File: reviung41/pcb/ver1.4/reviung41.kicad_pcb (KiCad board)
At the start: 2 copper layers, 253.3 x 107.1 mm, 111 parts, among them SW1 SW_PUSH, SW10 SW_PUSH, SW11 SW_PUSH, SW12 SW_PUSH, SW13 SW_PUSH, SW14 SW_PUSH, SW15 SW_PUSH, SW16 SW_PUSH, SW17 SW_PUSH, SW18 SW_PUSH, SW19 SW_PUSH, SW2 SW_PUSH, SW20 SW_PUSH, SW21 SW_PUSH, SW22 SW_PUSH, SW23 SW_PUSH, SW24 SW_PUSH, SW25 SW_PUSH, SW26 SW_PUSH, SW27 SW_PUSH, SW28 SW_PUSH, SW29 SW_PUSH, SW3 SW_PUSH, SW30 SW_PUSH, SW31 SW_PUSH, SW32 SW_PUSH, SW33 SW_PUSH, SW34 SW_PUSH, SW35 SW_PUSH, SW36 SW_PUSH, SW37 SW_PUSH, SW38 SW_PUSH, SW39 SW_2U_PUSH, SW4 SW_PUSH, SW40 SW_PUSH, SW41 SW_PUSH, SW5 SW_PUSH, SW6 SW_PUSH, SW7 SW_PUSH, SW8 SW_PUSH, SW9 SW_PUSH, U1 ProMicro

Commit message: Add KiCad 6 project for reviung41
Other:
- net class Default removed

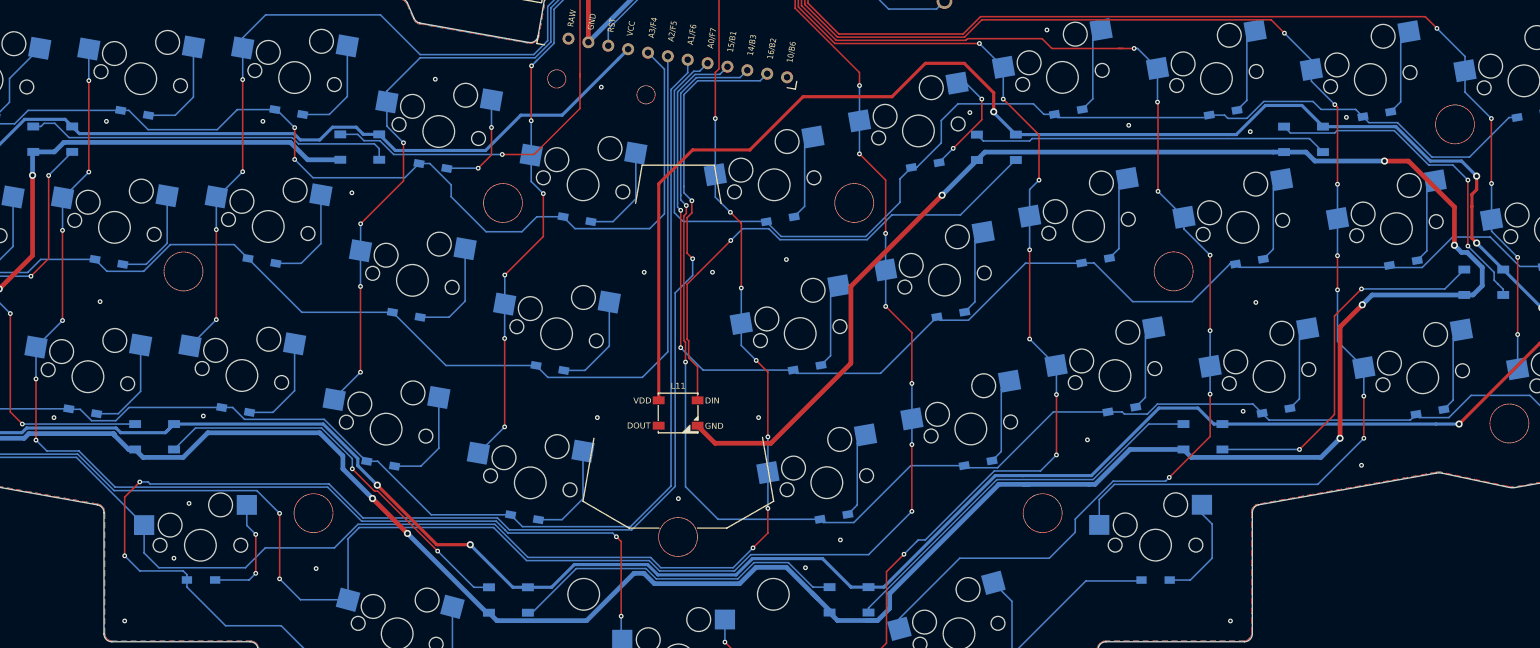
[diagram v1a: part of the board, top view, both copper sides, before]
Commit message: Cleanup zero length and redundant tracks
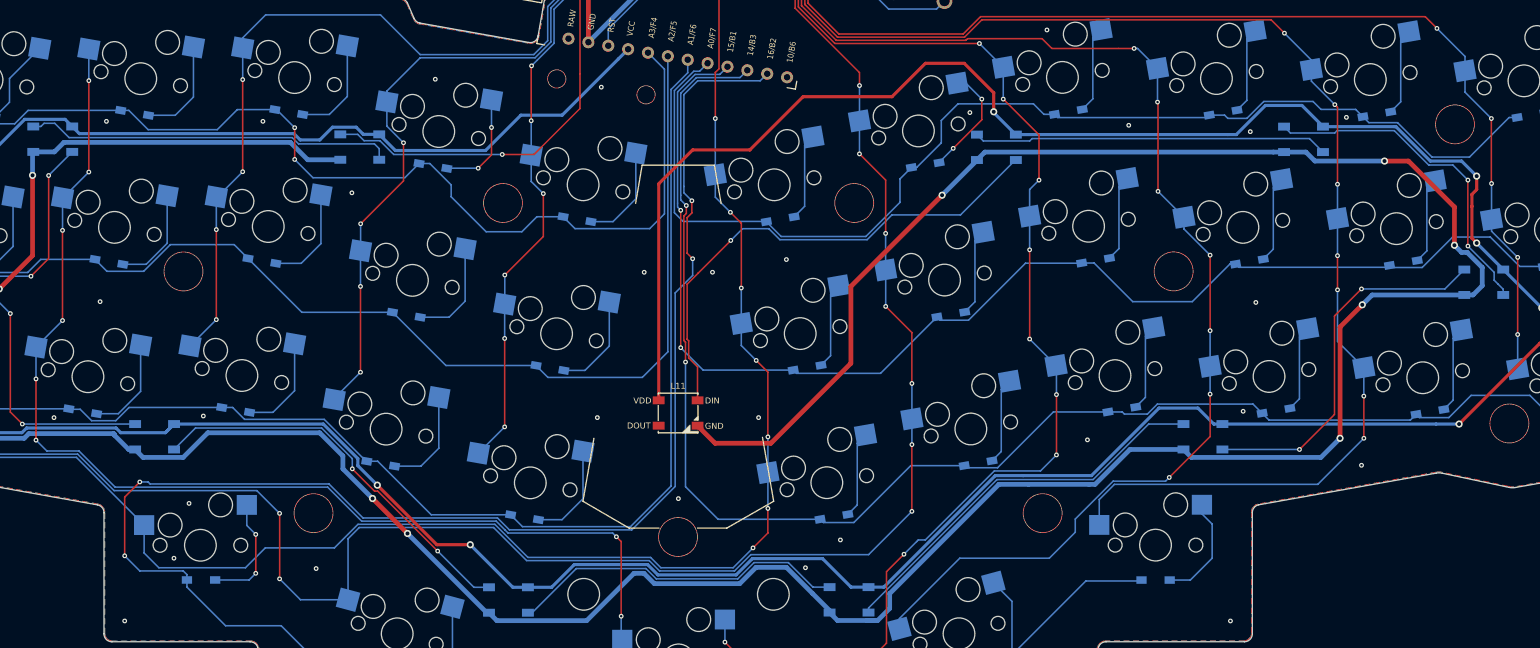
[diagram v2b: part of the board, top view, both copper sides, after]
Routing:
- net GND: track 541.9 -> 540.4 mm
- net Net-(D20-Pad2): track 15.6 -> 14.2 mm
- net col3: track 278.1 -> 276.6 mm
- net VCC: track 552.4 -> 551.8 mm
- net col5: track 231.4 -> 230.8 mm
